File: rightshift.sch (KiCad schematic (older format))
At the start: 0 parts

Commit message: Added right shift to schematic
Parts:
- added DRS1, DRS2, DRS3: 1N4148WS, symbol D
- added RRS1, RRS2, RRS3: 2.2k, symbol R
- added RS1, RS4, RS7: MX-1U, symbol MX-1U
- added RS2, RS3: MX-1.25U, symbol MX-1.25U
- added RS5, RS8: MX-1.75U, symbol MX-1.75U
- added RS6: MX-2.75U, symbol MX-2.75U
- added RS9: MX-2U, symbol MX-2U
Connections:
- new net: DRS1.1 (K), RS1.1 (COL), RS2.1 (COL), RS3.1 (COL)
- new net: RRS1.1, RS1.3 (LED), RS2.3 (LED), RS3.3 (LED)
- new net: DRS2.1 (K), RS4.1 (COL), RS5.1 (COL), RS6.1 (COL)
- new net: RRS2.1, RS4.3 (LED), RS5.3 (LED), RS6.3 (LED)
- new net: DRS3.1 (K), RS7.1 (COL), RS8.1 (COL), RS9.1 (COL)
- new net: RRS3.1, RS7.3 (LED), RS8.3 (LED), RS9.3 (LED)
- new net rightshift5V: RRS1.2, RRS2.2, RRS3.2
- new net rightshiftLEDGND: RS1.4 (LEDGND), RS2.4 (LEDGND), RS3.4 (LEDGND), RS4.4 (LEDGND), RS5.4 (LEDGND), RS6.4 (LEDGND), RS7.4 (LEDGND), RS8.4 (LEDGND), RS9.4 (LEDGND)
- new net rightshiftcol1: DRS1.2 (A)
- new net rightshiftcol2: DRS2.2 (A)
- new net rightshiftcol3: DRS3.2 (A)
- new net rightshiftrow: RS1.2 (ROW), RS2.2 (ROW), RS3.2 (ROW), RS4.2 (ROW), RS5.2 (ROW), RS6.2 (ROW), RS7.2 (ROW), RS8.2 (ROW), RS9.2 (ROW)

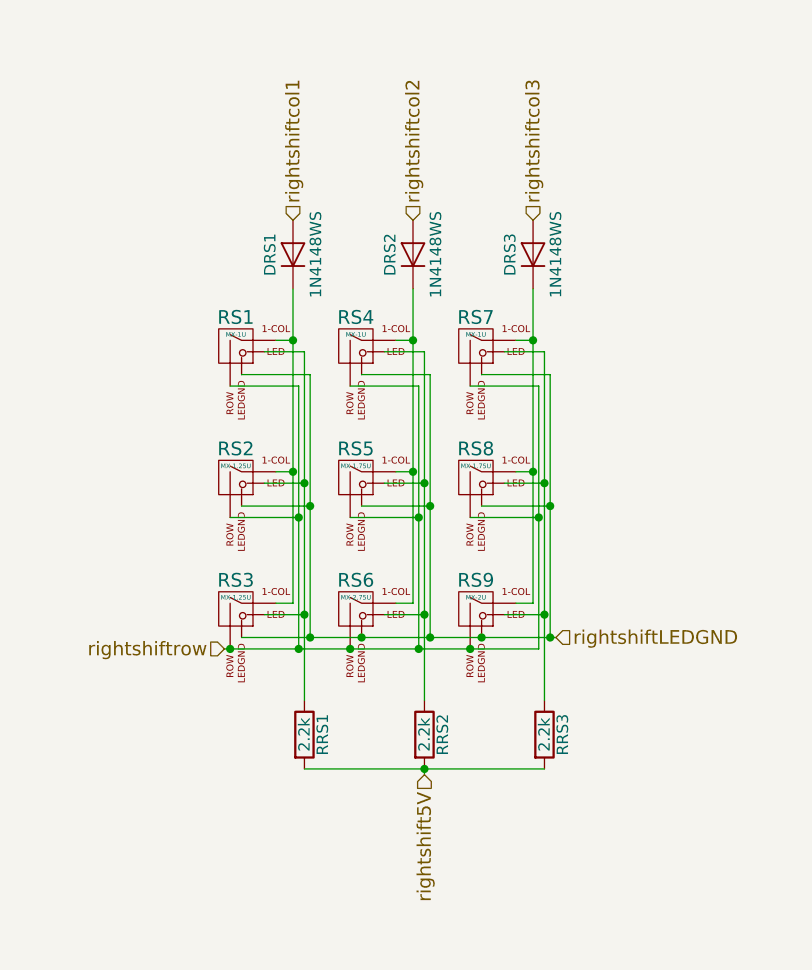
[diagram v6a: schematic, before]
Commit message: Hooked up right shift to matrix
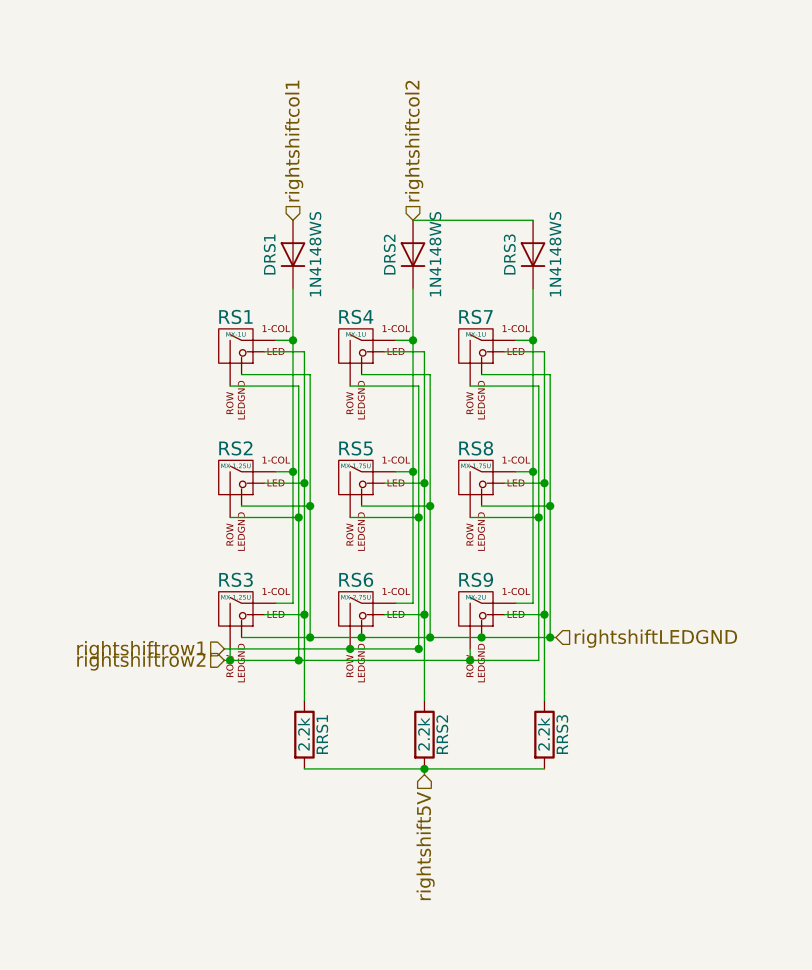
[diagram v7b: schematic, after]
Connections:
- net rightshiftcol3 is gone; now on net rightshiftcol2: DRS3.2 (A)
- net rightshiftrow renamed rightshiftrow2
- net rightshiftrow2: no longer RS4.2 (ROW), RS5.2 (ROW), RS6.2 (ROW)
- new net rightshiftrow1: RS4.2 (ROW), RS5.2 (ROW), RS6.2 (ROW)
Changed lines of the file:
@@
 $Descr A4 11693 8268
 encoding utf-8
-Sheet 2 7
+Sheet 3 7
 Title ""
 Date ""
@@
 	4775 2425 5075 2425
 Wire Wire Line
-	5075 2425 5075 3575
+	5075 2425 5075 3625
 Wire Wire Line
 	5075 3000 4775 3000
 Wire Wire Line
-	4750 3575 6125 3575
+	5600 3575 4750 3575
 Connection ~ 5075 3000
 Wire Wire Line
@@
 	5825 2425 6125 2425
 Wire Wire Line
-	6125 2425 6125 3575
+	6125 3625 6125 2425
 Wire Wire Line
 	6125 3000 5825 3000
 Connection ~ 6125 3000
 Connection ~ 5300 3575
-Connection ~ 5075 3575
-Connection ~ 5825 3575
 Connection ~ 5600 3575
 Wire Wire Line
@@
 Text HLabel 5575 1700 1    60   Input ~ 0
 rightshiftcol2
-Text HLabel 6100 1700 1    60   Input ~ 0
-rightshiftcol3
 Connection ~ 6100 2225
 Connection ~ 5575 2225
 Text HLabel 4750 3575 0    60   Input ~ 0
-rightshiftrow
-Connection ~ 4775 3575
+rightshiftrow1
 $Comp
 L R RRS1
@@
 rightshiftLEDGND
 Connection ~ 6175 3525
+Text HLabel 4750 3625 0    60   Input ~ 0
+rightshiftrow2
+Wire Wire Line
+	5575 1700 6100 1700
+Wire Wire Line
+	4775 3575 4775 3625
+Wire Wire Line
+	4750 3625 6125 3625
+Wire Wire Line
+	5825 3625 5825 3575
+Connection ~ 4775 3625
+Connection ~ 5075 3625
+Connection ~ 5825 3625
 $EndSCHEMATC
